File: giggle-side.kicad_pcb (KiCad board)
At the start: 2 copper layers, 97.5 x 97 mm, 41 parts, among them J2 CONN_05X2SHD

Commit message: placed the switches and stuff in the main, i guess.
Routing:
- net N-col-0: track 60.2 -> 143.7 mm
- net N-col-1: track 63.2 -> 127.3 mm
- net N-col-2: track 63.2 -> 110.8 mm
- net N-col-3: track 63.2 -> 94.3 mm
- net N-col-8: track 0.00 -> 7.65 mm
- net N-col-7: track 0.00 -> 7.65 mm
- net N-col-6: track 0.00 -> 7.65 mm
- net N-col-5: track 0.00 -> 7.65 mm
- net N-col-11: track 0.00 -> 7.65 mm
- net N-diode-19: track 7.65 -> 0.00 mm
- net N-diode-14: track 7.65 -> 0.00 mm
- net N-diode-11: track 7.65 -> 0.00 mm
- net N-col-9: track 0.00 -> 7.65 mm
- net N-col-12: track 0.00 -> 7.65 mm
- net N-col-10: track 0.00 -> 7.65 mm
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
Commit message: finished main side.
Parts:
- moved d2:0 10.0 mm to (84.1, 47.1)
- moved d2:1 10.0 mm to (84.1, 66.2)
- moved d2:2 10.0 mm to (84.1, 85.2)
- moved d2:3 10.0 mm to (84.1, 104.2)
- moved sw2:0 10.0 mm to (76.1, 47.1)
- moved sw2:1 10.0 mm to (76.1, 66.2)
- moved sw2:2 10.0 mm to (76.1, 85.2)
- moved sw2:3 10.0 mm to (76.1, 104.2)
- moved d1:0 5.00 mm to (65.1, 52.1)
- moved d1:1 5.00 mm to (65.1, 71.2)
- moved d1:2 5.00 mm to (65.1, 90.2)
- moved d1:3 5.00 mm to (65.1, 109.2)
- moved d3:0 5.00 mm to (103.1, 52.1)
- moved d3:1 5.00 mm to (103.1, 71.2)
- moved d3:2 5.00 mm to (103.1, 90.2)
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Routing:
- net N-col-4: track 102.9 -> 99.9 mm
- net N-col-0: track 143.7 -> 146.6 mm
- net N-col-3: track 94.3 -> 92.3 mm
- net N-col-2: track 110.8 -> 109.6 mm
- net N-row-1: track 136.0 -> 137.0 mm
- net N-row-3: track 182.1 -> 183.0 mm
- net N-col-1: track 127.3 -> 128.0 mm
- net N-row-0: track 112.8 -> 112.3 mm

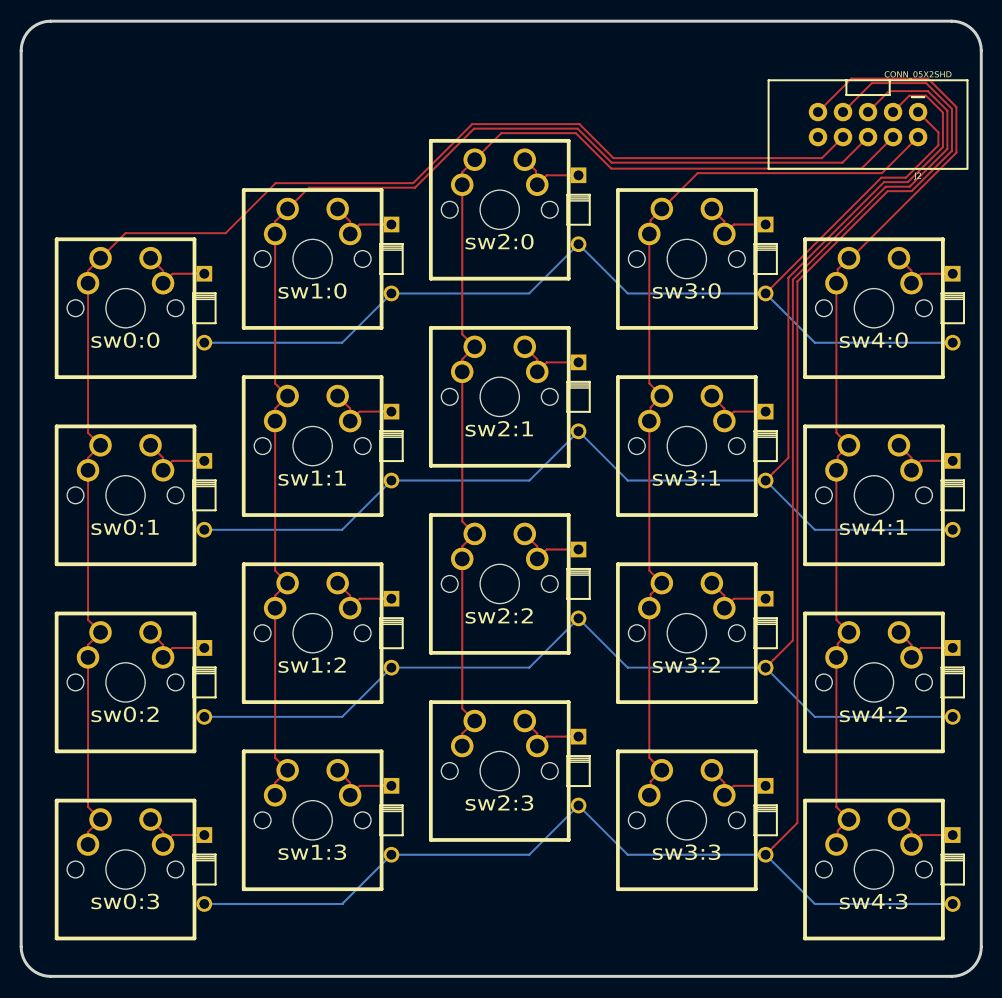
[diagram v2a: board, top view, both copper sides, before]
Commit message: some thing.
1. added another connector on side part.
2. nicer traces.
3. added the giggle text.
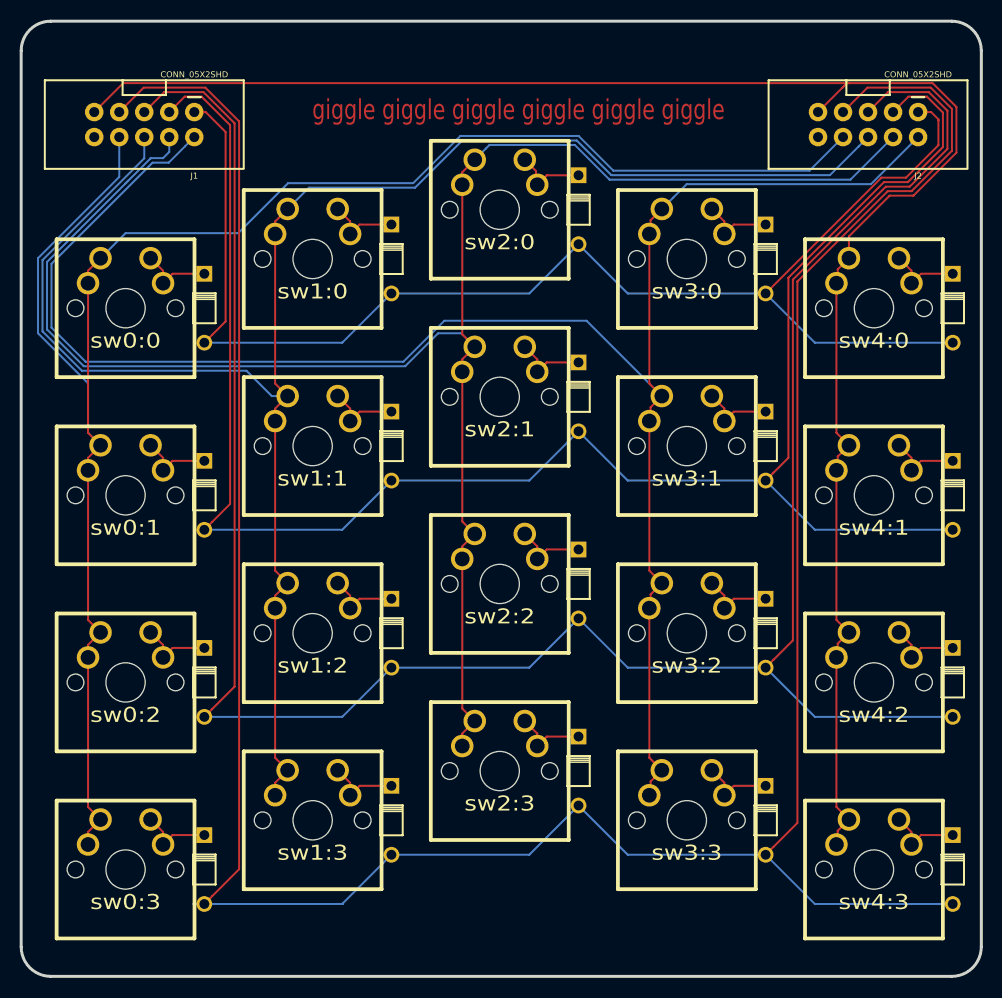
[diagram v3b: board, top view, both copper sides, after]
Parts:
- added J1: CONN_05X2SHD, connector-shrouded, F.Cu at (40.0, 38.5)
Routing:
- net N-row-3: track 183.0 -> 279.3 mm
- net N-col-3: track 92.3 -> 188.0 mm
- net N-col-4: track 99.9 -> 179.6 mm
- net N-row-2: track 159.7 -> 232.5 mm
- net N-col-2: track 109.6 -> 182.3 mm
- net N-col-1: track 128.0 -> 179.7 mm
- net N-row-1: track 137.0 -> 187.1 mm
- net N-col-0: track 146.6 -> 184.0 mm
- net N-row-0: track 112.3 -> 139.4 mm
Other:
- board text added: "giggle giggle giggle giggle giggle giggle"
